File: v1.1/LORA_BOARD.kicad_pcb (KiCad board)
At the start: 2 copper layers, 32 x 96.8 mm, 53 parts, among them J2 U.FL, J3 UART, J4 I2C, J5 ICSP, Q1 BC817, Q2 DMG2301L, U2 TS2940-3.3, U3 MCP73831-2-OT

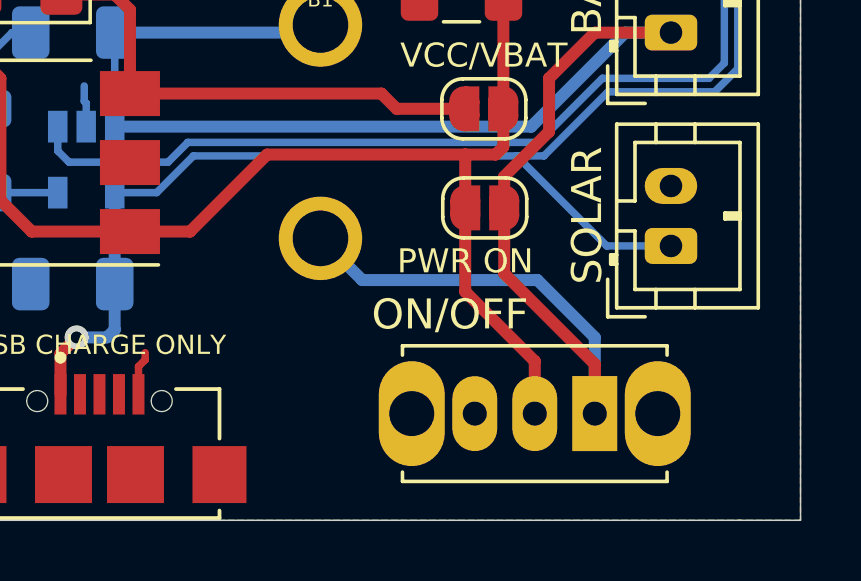
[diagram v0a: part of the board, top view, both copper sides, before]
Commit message: Poprawienie opisu włącznika zasilania; Dodanie plików produkcyjnych GERBER.
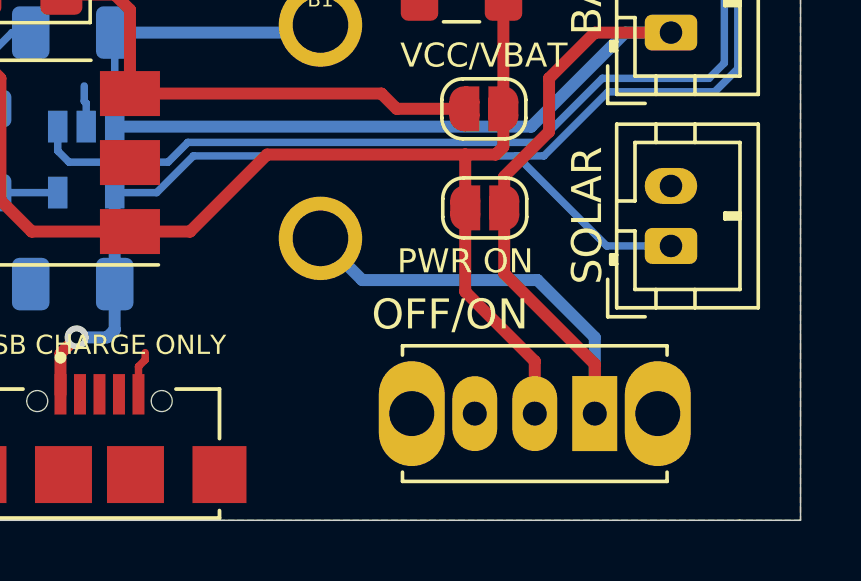
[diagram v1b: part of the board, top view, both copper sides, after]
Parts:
- renumbered ON/OFF to OFF/ON
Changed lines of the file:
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@@
       (drillshape 0)
       (scaleselection 1)
-      (outputdirectory "GERBER/"))
+      (outputdirectory "Pliki_produkcyjne/"))
   )
   (net 0 "")
@@
     (descr "CuK miniature slide switch, OS series, SPDT, https://www.ckswitches.com/media/1428/os.pdf")
     (tags "switch SPDT")
-    (fp_text reference ON/OFF (at 4.826 3.302) (layer F.SilkS)
+    (fp_text reference OFF/ON (at 4.826 3.302) (layer F.SilkS)
       (effects (font (size 1 1) (thickness 0.15)))
     )
